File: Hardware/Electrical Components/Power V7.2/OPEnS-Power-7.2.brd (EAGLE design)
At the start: 25 x 54 mm, 26 parts, among them U2 DS3231SNT&R, U3 LM2575SX-5.0/NOPB

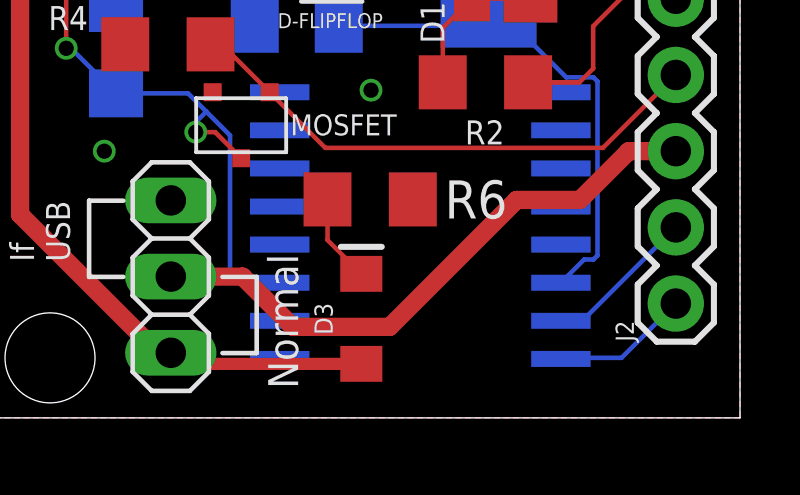
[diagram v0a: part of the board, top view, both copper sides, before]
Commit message: Bug fix for Powerboard 7.2V
Changed R5 and R2 value to protect against RTC_READ floating when feather is as sleep.
Added C4 capacitor to further protect against floating RTC_READ.
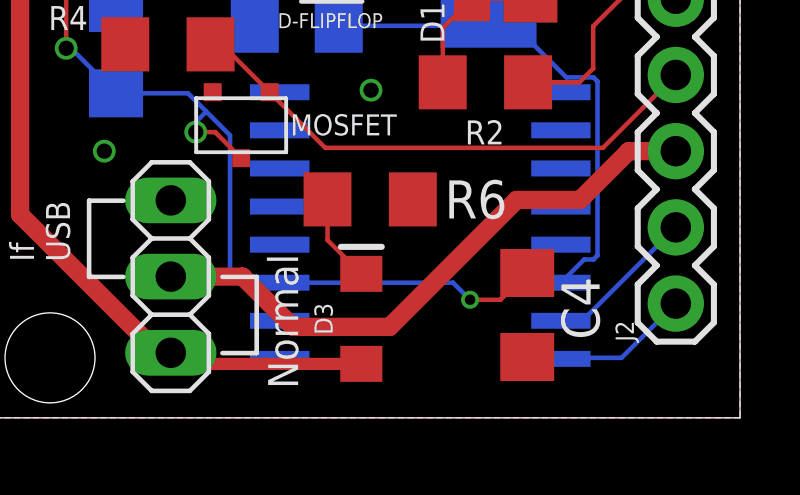
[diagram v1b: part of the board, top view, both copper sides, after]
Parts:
- added C4: 0.1uF, adafruit:C1206
- R2: value 300k -> 30k
- R5: value 10K -> 300k
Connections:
- net GND: now also C4.2
- net RTC_INT: now also C4.1
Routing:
- net RTC_INT: track 49.3 -> 58.1 mm, vias 2 -> 3
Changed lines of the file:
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@@
 <attribute name="VALUE" x="7.327" y="17.963" size="1.27" layer="27" rot="R180"/>
 </element>
-<element name="R2" library="adafruit" library_urn="urn:adsk.eagle:library:420" package="R1206" package3d_urn="urn:adsk.eagle:package:6240569/1" value="300k" x="16.513" y="11.185" smashed="yes" rot="R180">
+<element name="R2" library="adafruit" library_urn="urn:adsk.eagle:library:420" package="R1206" package3d_urn="urn:adsk.eagle:package:6240569/1" value="30k" x="16.513" y="11.185" smashed="yes" rot="R180">
 <attribute name="NAME" x="17.148" y="9.915" size="0.8" layer="25" rot="R180"/>
 <attribute name="VALUE" x="17.783" y="9.058" size="0.8" layer="27" rot="R180"/>
@@
 <attribute name="VALUE" x="4.533" y="10.037" size="1.27" layer="27"/>
 </element>
-<element name="R5" library="adafruit" library_urn="urn:adsk.eagle:library:420" package="R1206" package3d_urn="urn:adsk.eagle:package:6240569/1" value="10K" x="4.2" y="12.24" smashed="yes" rot="MR270">
+<element name="R5" library="adafruit" library_urn="urn:adsk.eagle:library:420" package="R1206" package3d_urn="urn:adsk.eagle:package:6240569/1" value="300k" x="4.2" y="12.24" smashed="yes" rot="MR270">
 <attribute name="NAME" x="2.803" y="11.875" size="0.8" layer="26" rot="MR270"/>
 <attribute name="VALUE" x="6.613" y="13.637" size="1.27" layer="28" rot="MR270"/>
@@
 <attribute name="NAME" x="18.4658" y="54.2798" size="1.27" layer="25" ratio="10"/>
 <attribute name="VALUE" x="18.542" y="49.276" size="1.27" layer="27"/>
+</element>
+<element name="C4" library="adafruit" library_urn="urn:adsk.eagle:library:420" package="C1206" package3d_urn="urn:adsk.eagle:package:6240335/1" value="0.1uF" x="17.907" y="3.429" smashed="yes" rot="R270">
+<attribute name="NAME" x="19.05" y="4.699" size="1.27" layer="25" rot="R270"/>
+<attribute name="VALUE" x="15.494" y="4.699" size="1.27" layer="27" rot="R270"/>
 </element>
 </elements>
@@
 <wire x1="2.699" y1="12.319" x2="4.2" y2="10.818" width="0.1524" layer="16"/>
 <wire x1="0.7874" y1="42.320325" x2="0.7874" y2="36.419675" width="0.1524" layer="1"/>
+<contactref element="C4" pad="1"/>
+<wire x1="9.6567" y1="4.505" x2="15.434" y2="4.505" width="0.1524" layer="16"/>
+<wire x1="15.434" y1="4.505" x2="16.002" y2="3.937" width="0.1524" layer="16"/>
+<via x="16.002" y="3.937" extent="1-16" drill="0.35"/>
+<wire x1="16.002" y1="3.937" x2="17.015" y2="3.937" width="0.1524" layer="1"/>
+<wire x1="17.015" y1="3.937" x2="17.907" y2="4.829" width="0.1524" layer="1"/>
 </signal>
 <signal name="GND">
@@
 <via x="3.81" y="8.89" extent="1-16" drill="0.508"/>
 <via x="12.7" y="10.922" extent="1-16" drill="0.508"/>
+<contactref element="C4" pad="2"/>
 </signal>
 <signal name="EN_" class="3">
